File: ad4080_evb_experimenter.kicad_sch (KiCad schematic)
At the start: 61 parts, among them J1 Conn_Coaxial, J2 AudioJack2_Ground, J3 Conn_02x02_Odd_Even, J4 Conn_Coaxial, J5 Conn_Coaxial, SW1 SW_Coded_SH-7050, U1 LT1678, U2 74LS163, U3 74HC04, X1 CXO_DIP8

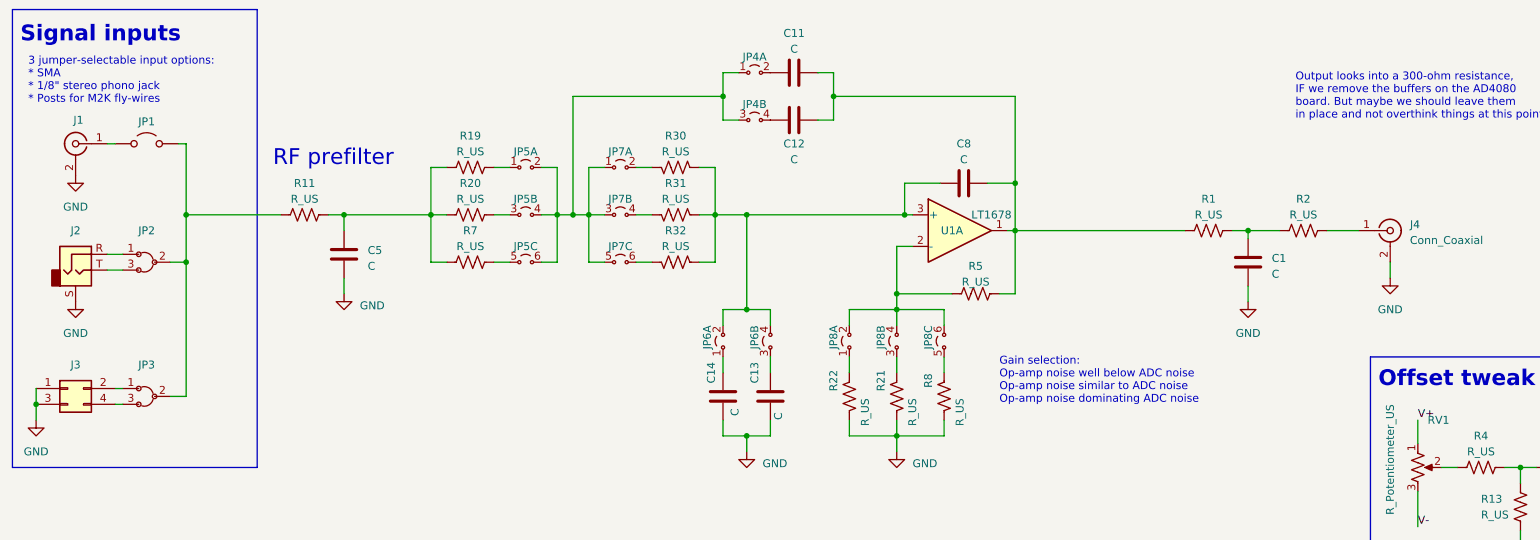
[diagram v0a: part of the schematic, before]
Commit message: Reduced unused space, fix DRC errors
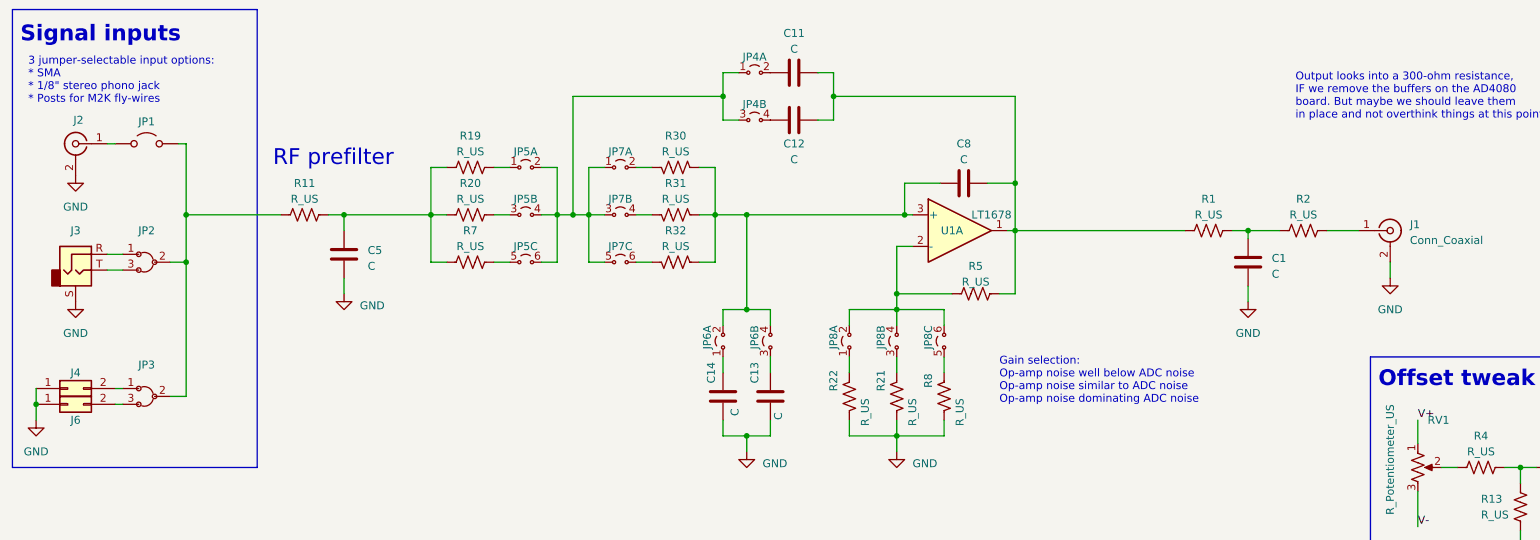
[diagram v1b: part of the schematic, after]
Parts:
- removed J3: Conn_02x02_Odd_Even, Connector_PinHeader_2.54mm:PinHeader_2x02_P2.54mm_Vertical, symbol Connector_Generic:Conn_02x02_Odd_Even
- added J4, J6: Conn_02x01, Connector_PinHeader_2.54mm:PinHeader_1x02_P2.54mm_Vertical, symbol Connector_Generic:Conn_02x01
- renumbered J4 to J1, J1 to J2, J2 to J3
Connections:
- net GND: now also J4.1 (Pin_1), J6.1 (Pin_1)
- net at JP3.1: now also J4.2 (Pin_2)
- net at JP3.3: now also J6.2 (Pin_2)
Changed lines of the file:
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@@
 	)
 	(junction
-		(at 17.78 77.47)
-		(diameter 0)
-		(color 0 0 0 0)
-	)
-	(junction
 		(at 49.53 120.65)
 		(diameter 0)
@@
 	)
 	(junction
+		(at 17.78 77.47)
+		(diameter 0)
+		(color 0 0 0 0)
+	)
+	(junction
 		(at 41.91 54.61)
 		(diameter 0)
@@
 	(wire
 		(pts
+			(xy 17.78 77.47) (xy 17.78 80.01)
+		)
+		(stroke
+			(width 0)
+			(type default)
+		)
+	)
+	(wire
+		(pts
 			(xy 62.23 120.65) (xy 57.15 120.65)
 		)
@@
 	(wire
 		(pts
-			(xy 17.78 77.47) (xy 17.78 80.01)
-		)
-		(stroke
-			(width 0)
-			(type default)
-		)
-	)
-	(wire
-		(pts
 			(xy 144.78 177.165) (xy 144.78 178.435)
 		)
@@
 		(dnp no)
 		(fields_autoplaced yes)
-		(property "Reference" "J4"
+		(property "Reference" "J1"
 			(at 238.76 48.5531 0)
 			(effects
@@
 			(project "ad4080_evb_experimenter"
 				(path "/b69282a1-dfbe-4b32-8ce1-82537d42439c"
-					(reference "J4")
+					(reference "J1")
 					(unit 1)
 				)
@@
 	)
 	(symbol
+		(lib_id "Connector_Generic:Conn_02x01")
+		(at 22.86 74.93 0)
+		(unit 1)
+		(exclude_from_sim no)
+		(in_bom yes)
+		(on_board yes)
+		(dnp no)
+		(property "Reference" "J4"
+			(at 24.13 72.39 0)
+			(effects
+				(font
+					(size 1.27 1.27)
+				)
+			)
+		)
+		(property "Value" "Conn_02x01"
+			(at 26.67 69.85 0)
+			(effects
+				(font
+					(size 1.27 1.27)
+				)
+				(hide yes)
+			)
+		)
+		(property "Footprint" "Connector_PinHeader_2.54mm:PinHeader_1x02_P2.54mm_Vertical"
+			(at 22.86 74.93 0)
+			(effects
+				(font
+					(size 1.27 1.27)
+				)
+				(hide yes)
+			)
+		)
+		(property "Datasheet" "~"
+			(at 22.86 74.93 0)
+			(effects
+				(font
+					(size 1.27 1.27)
+				)
+				(hide yes)
+			)
+		)
+		(property "Description" "Generic connector, double row, 02x01, this symbol is compatible with counter-clockwise, top-bottom and odd-even numbering schemes., script generated (kicad-library-utils/schlib/autogen/connector/)"
+			(at 22.86 74.93 0)
+			(effects
+				(font
+					(size 1.27 1.27)
+				)
+				(hide yes)
+			)
+		)
+		(pin "2"
+		)
+		(pin "1"
+		)
+		(instances
+			(project "ad4080_evb_experimenter"
+				(path "/b69282a1-dfbe-4b32-8ce1-82537d42439c"
+					(reference "J4")
+					(unit 1)
+				)
+			)
+		)
+	)
+	(symbol
 		(lib_id "74xx:74HC04")
 		(at 128.27 174.625 0)
@@
 		(on_board yes)
 		(dnp no)
-		(property "Reference" "J1"
+		(property "Reference" "J2"
 			(at 25.4 31.75 0)
 			(effects
@@
 			(project "ad4080_evb_experimenter"
 				(path "/b69282a1-dfbe-4b32-8ce1-82537d42439c"
-					(reference "J1")
+					(reference "J2")
 					(unit 1)
 				)
@@
 	)
 	(symbol
-		(lib_id "Connector_Generic:Conn_02x02_Odd_Even")
-		(at 22.86 74.93 0)
-		(unit 1)
-		(exclude_from_sim no)
-		(in_bom yes)
-		(on_board yes)
-		(dnp no)
-		(property "Reference" "J3"
-			(at 24.13 71.12 0)
-			(effects
-				(font
-					(size 1.27 1.27)
-				)
-			)
-		)
-		(property "Value" "Conn_02x02_Odd_Even"
-			(at 24.13 71.12 0)
-			(effects
-				(font
-					(size 1.27 1.27)
-				)
-				(hide yes)
-			)
-		)
-		(property "Footprint" "Connector_PinHeader_2.54mm:PinHeader_2x02_P2.54mm_Vertical"
-			(at 22.86 74.93 0)
-			(effects
-				(font
-					(size 1.27 1.27)
-				)
-				(hide yes)
-			)
-		)
-		(property "Datasheet" "~"
-			(at 22.86 74.93 0)
-			(effects
-				(font
-					(size 1.27 1.27)
-				)
-				(hide yes)
-			)
-		)
-		(property "Description" "Generic connector, double row, 02x02, odd/even pin numbering scheme (row 1 odd numbers, row 2 even numbers), script generated (kicad-library-utils/schlib/autogen/connector/)"
-			(at 22.86 74.93 0)
-			(effects
-				(font
-					(size 1.27 1.27)
-				)
-				(hide yes)
-			)
-		)
-		(pin "4"
-		)
-		(pin "3"
-		)
-		(pin "1"
-		)
-		(pin "2"
-		)
-		(instances
-			(project "ad4080_evb_experimenter"
-				(path "/b69282a1-dfbe-4b32-8ce1-82537d42439c"
-					(reference "J3")
-					(unit 1)
-				)
-			)
-		)
-	)
-	(symbol
 		(lib_id "Amplifier_Operational:LM358")
 		(at 166.37 49.53 0)
@@
 	)
 	(symbol
+		(lib_id "Connector_Generic:Conn_02x01")
+		(at 22.86 77.47 0)
+		(unit 1)
+		(exclude_from_sim no)
+		(in_bom yes)
+		(on_board yes)
+		(dnp no)
+		(property "Reference" "J6"
+			(at 24.13 80.01 0)
+			(effects
+				(font
+					(size 1.27 1.27)
+				)
+			)
+		)
+		(property "Value" "Conn_02x01"
+			(at 27.94 82.55 0)
+			(effects
+				(font
+					(size 1.27 1.27)
+				)
+				(hide yes)
+			)
+		)
+		(property "Footprint" "Connector_PinHeader_2.54mm:PinHeader_1x02_P2.54mm_Vertical"
+			(at 22.86 77.47 0)
+			(effects
+				(font
+					(size 1.27 1.27)
+				)
+				(hide yes)
+			)
+		)
+		(property "Datasheet" "~"
+			(at 22.86 77.47 0)
+			(effects
+				(font
+					(size 1.27 1.27)
+				)
+				(hide yes)
+			)
+		)
+		(property "Description" "Generic connector, double row, 02x01, this symbol is compatible with counter-clockwise, top-bottom and odd-even numbering schemes., script generated (kicad-library-utils/schlib/autogen/connector/)"
+			(at 22.86 77.47 0)
+			(effects
+				(font
+					(size 1.27 1.27)
+				)
+				(hide yes)
+			)
+		)
+		(pin "2"
+		)
+		(pin "1"
+		)
+		(instances
+			(project "ad4080_evb_experimenter"
+				(path "/b69282a1-dfbe-4b32-8ce1-82537d42439c"
+					(reference "J6")
+					(unit 1)
+				)
+			)
+		)
+	)
+	(symbol
 		(lib_id "Device:R_US")
 		(at 256.54 93.98 180)
@@
 		(on_board yes)
 		(dnp no)
-		(property "Reference" "J2"
+		(property "Reference" "J3"
 			(at 24.13 49.53 0)
 			(effects
@@
 			(project "ad4080_evb_experimenter"
 				(path "/b69282a1-dfbe-4b32-8ce1-82537d42439c"
-					(reference "J2")
+					(reference "J3")
 					(unit 1)
 				)

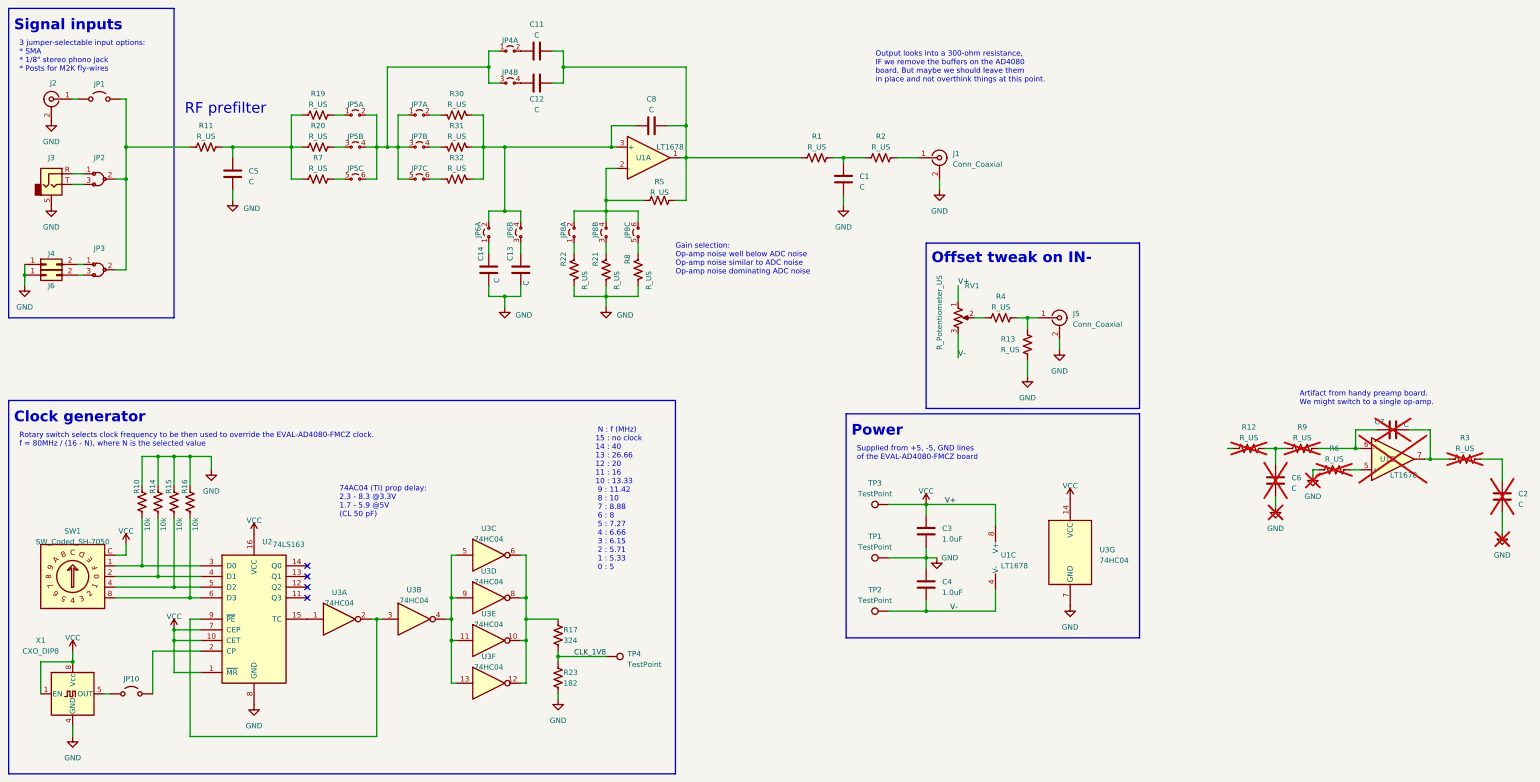
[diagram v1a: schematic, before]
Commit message: Single opamp, decouple digital power, selectable attenuation, routing and silkscreen tweaks
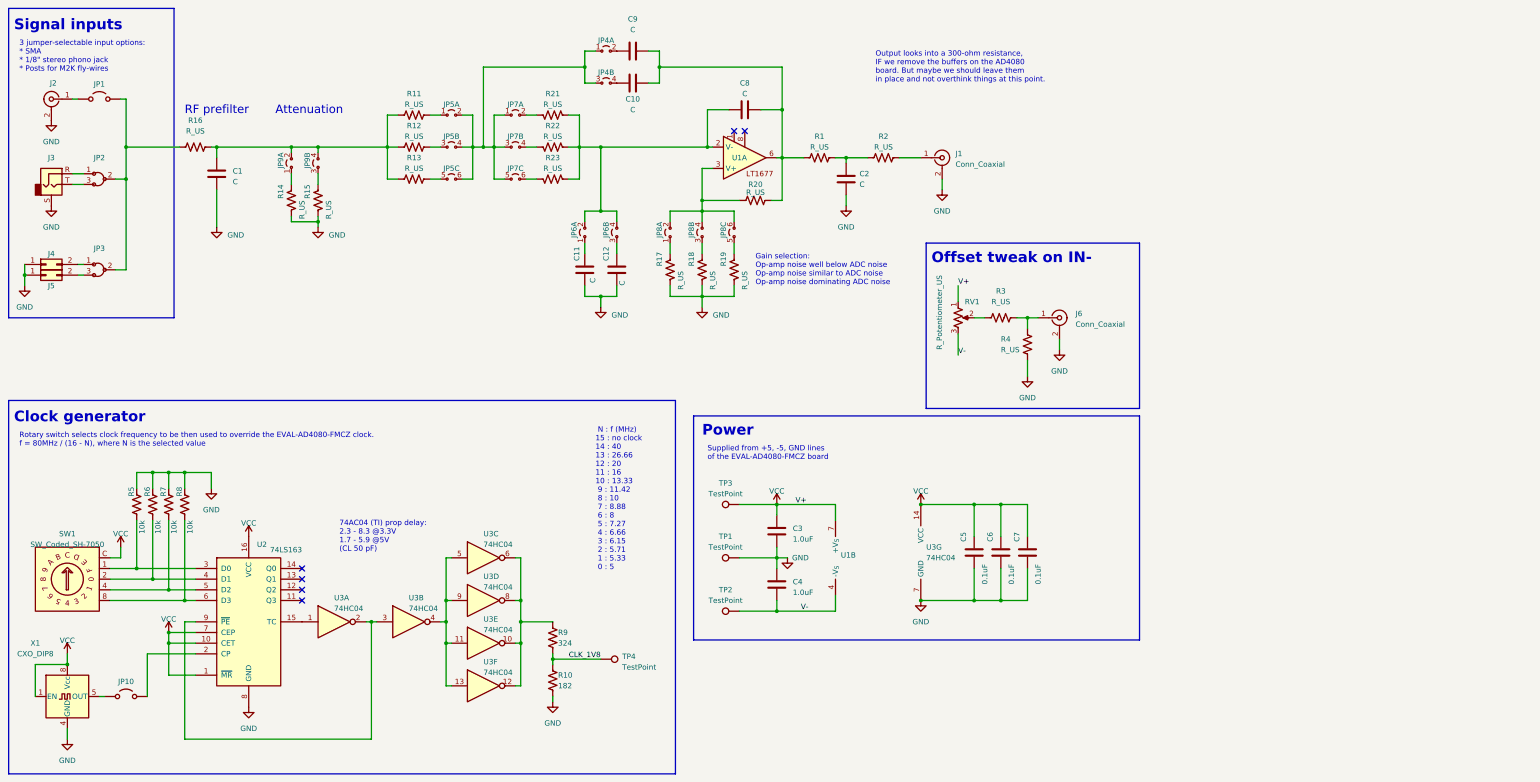
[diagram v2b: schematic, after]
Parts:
- removed C2: C, Capacitor_THT:C_Rect_L7.2mm_W2.5mm_P5.00mm_FKS2_FKP2_MKS2_MKP2, symbol Device:C
- removed R12, R3, R6, R9: R_US, Resistor_THT:R_Axial_DIN0207_L6.3mm_D2.5mm_P10.16mm_Horizontal, symbol Device:R_US
- removed U1: LT1678, Package_DIP:DIP-8_W7.62mm_LongPads, symbol Amplifier_Operational:LM358
- added C5: 0.1uF, Capacitor_THT:C_Rect_L7.2mm_W2.5mm_P5.00mm_FKS2_FKP2_MKS2_MKP2, symbol Device:C
- added JP9: ~, Connector_PinHeader_2.54mm:PinHeader_2x02_P2.54mm_Vertical, symbol FTC2024:JumperBlock_2x2
- added R14, R15: R_US, Resistor_THT:R_Axial_DIN0207_L6.3mm_D2.5mm_P10.16mm_Horizontal, symbol Device:R_US
- added U1: ~, Package_DIP:DIP-8_W7.62mm, symbol FTC2024:LT1677
- C6, C7: value C -> 0.1uF; now fitted; now in the parts list
- JP2, JP3: symbol FTC2024:Jumper3 -> FTC2024:Jumper_3
- renumbered C5 to C1, C12 to C10, C14 to C11, C13 to C12, C1 to C2, C11 to C9, J6 to J5, J5 to J6, R23 to R10, R19 to R11, R20 to R12, R7 to R13, R11 to R16, R22 to R17, R21 to R18, R8 to R19, R5 to R20, R30 to R21, R31 to R22, R32 to R23, R4 to R3, R13 to R4, R10 to R5, R14 to R6, R15 to R7, R16 to R8, R17 to R9
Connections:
- net GND: now also C7.2, C5.2, R14.1, R15.1
- net V-: now also U1.4 (-V_{S})
- net VCC: now also C6.1, C7.1, C5.1, U1.7 (+V_{S})
- net at JP8.2, JP8.4, JP8.6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: now also U1.3 (V+)
- net at C8.1, JP6.2, JP6.4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: now also U1.2 (V-)
- net at C1.1, R11.1, R12.1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: now also JP9.2, JP9.4
- net at C10.2, C8.2, C9.2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: now also U1.6
- new net: JP9.1, R14.2
- new net: JP9.3, R15.2
- no-connect marks 4 -> 6
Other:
- note added: "Attenuation"
- note removed: "Artifact from handy preamp board. We might switch to a single op-amp."
- moved on the sheet: C1, C10, C11, C12, C2, C3, C4, C8, C9, J1, JP10, JP4A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

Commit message: Fix flipped opamp inputs
Signed-off-by: Ioan Dragomir <ioan.dragomir@analog.com>
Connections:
- net at JP8.2, JP8.4, JP8.6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: now also U1.2 (V-); no longer U1.3 (V+)
- net at C8.1, JP6.2, JP6.4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: now also U1.3 (V+); no longer U1.2 (V-)
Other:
- moved on the sheet: U1A
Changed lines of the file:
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@@
 	)
 	(no_connect
-		(at 186.69 43.18)
+		(at 186.69 55.88)
 	)
 	(no_connect
-		(at 189.23 43.18)
+		(at 189.23 55.88)
 	)
 	(no_connect
@@
 		(lib_id "FTC2024:LT1677")
 		(at 184.15 49.53 0)
+		(mirror x)
 		(unit 1)
 		(exclude_from_sim no)
@@
 		)
 		(property "Value" "~"
-			(at 190.1685 58.42 0)
+			(at 190.1685 40.64 0)
 			(effects
 				(font

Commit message: Change test points to smaller Keystone Miniature
Signed-off-by: Ioan Dragomir <ioan.dragomir@analog.com>
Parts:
- TP1, TP2, TP3: footprint TestPoint:TestPoint_Plated_Hole_D3.0mm -> TestPoint:TestPoint_Keystone_5005-5009_Compact
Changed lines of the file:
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@@
 			)
 		)
-		(property "Footprint" "TestPoint:TestPoint_Plated_Hole_D3.0mm"
+		(property "Footprint" "TestPoint:TestPoint_Keystone_5005-5009_Compact"
 			(at 187.96 152.4 0)
 			(effects
@@
 			)
 		)
-		(property "Footprint" "TestPoint:TestPoint_Plated_Hole_D3.0mm"
+		(property "Footprint" "TestPoint:TestPoint_Keystone_5005-5009_Compact"
 			(at 187.96 139.7 0)
 			(effects
@@
 			)
 		)
-		(property "Footprint" "TestPoint:TestPoint_Plated_Hole_D3.0mm"
+		(property "Footprint" "TestPoint:TestPoint_Keystone_5005-5009_Compact"
 			(at 187.96 127 0)
 			(effects

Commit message: Add mounting holes, 3mm
Signed-off-by: Ioan Dragomir <ioan.dragomir@analog.com>
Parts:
- added H1, H2: MountingHole_Pad, MountingHole:MountingHole_3mm_Pad, symbol Mechanical:MountingHole_Pad
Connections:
- net GND: now also H1.1, H2.1
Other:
- note added: "Mounting holes"
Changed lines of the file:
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@@
 	)
 	(junction
+		(at 19.05 99.06)
+		(diameter 0)
+		(color 0 0 0 0)
+	)
+	(junction
 		(at 168.91 27.94)
 		(diameter 0)
@@
 	(wire
 		(pts
+			(xy 19.05 99.06) (xy 24.13 99.06)
+		)
+		(stroke
+			(width 0)
+			(type default)
+		)
+	)
+	(wire
+		(pts
 			(xy 135.89 144.78) (xy 135.89 154.94)
 		)
@@
 		)
 	)
+	(text "Mounting holes"
+		(exclude_from_sim no)
+		(at 22.86 91.44 0)
+		(effects
+			(font
+				(size 1.27 1.27)
+			)
+		)
+	)
 	(text "Supplied from +5, -5, GND lines\nof the EVAL-AD4080-FMCZ board"
 		(exclude_from_sim no)
@@
 	)
 	(symbol
+		(lib_id "Mechanical:MountingHole_Pad")
+		(at 19.05 96.52 0)
+		(unit 1)
+		(exclude_from_sim yes)
+		(in_bom no)
+		(on_board yes)
+		(dnp no)
+		(property "Reference" "H1"
+			(at 21.59 93.9799 0)
+			(effects
+				(font
+					(size 1.27 1.27)
+				)
+				(justify left)
+				(hide yes)
+			)
+		)
+		(property "Value" "MountingHole_Pad"
+			(at 10.16 91.44 0)
+			(effects
+				(font
+					(size 1.27 1.27)
+				)
+				(justify left)
+				(hide yes)
+			)
+		)
+		(property "Footprint" "MountingHole:MountingHole_3mm_Pad"
+			(at 19.05 96.52 0)
+			(effects
+				(font
+					(size 1.27 1.27)
+				)
+				(hide yes)
+			)
+		)
+		(property "Datasheet" "~"
+			(at 19.05 96.52 0)
+			(effects
+				(font
+					(size 1.27 1.27)
+				)
+				(hide yes)
+			)
+		)
+		(property "Description" "Mounting Hole with connection"
+			(at 19.05 96.52 0)
+			(effects
+				(font
+					(size 1.27 1.27)
+				)
+				(hide yes)
+			)
+		)
+		(pin "1"
+		)
+		(instances
+			(project "ad4080_evb_experimenter"
+				(path "/b69282a1-dfbe-4b32-8ce1-82537d42439c"
+					(reference "H1")
+					(unit 1)
+				)
+			)
+		)
+	)
+	(symbol
+		(lib_id "power:GND")
+		(at 19.05 99.06 0)
+		(unit 1)
+		(exclude_from_sim no)
+		(in_bom yes)
+		(on_board yes)
+		(dnp no)
+		(fields_autoplaced yes)
+		(property "Reference" "#PWR09"
+			(at 19.05 105.41 0)
+			(effects
+				(font
+					(size 1.27 1.27)
+				)
+				(hide yes)
+			)
+		)
+		(property "Value" "GND"
+			(at 21.59 100.965 0)
+			(effects
+				(font
+					(size 1.27 1.27)
+				)
+				(justify left)
+			)
+		)
+		(property "Footprint" ""
+			(at 19.05 99.06 0)
+			(effects
+				(font
+					(size 1.27 1.27)
+				)
+				(hide yes)
+			)
+		)
+		(property "Datasheet" ""
+			(at 19.05 99.06 0)
+			(effects
+				(font
+					(size 1.27 1.27)
+				)
+				(hide yes)
+			)
+		)
+		(property "Description" ""
+			(at 19.05 99.06 0)
+			(effects
+				(font
+					(size 1.27 1.27)
+				)
+				(hide yes)
+			)
+		)
+		(pin "1"
+		)
+		(instances
+			(project "ad4080_evb_experimenter"
+				(path "/b69282a1-dfbe-4b32-8ce1-82537d42439c"
+					(reference "#PWR09")
+					(unit 1)
+				)
+			)
+		)
+	)
+	(symbol
 		(lib_id "Device:R_US")
 		(at 110.49 54.61 90)
@@
 					(unit 1)
 				)
+			)
+		)
+	)
+	(symbol
+		(lib_id "Mechanical:MountingHole_Pad")
+		(at 24.13 96.52 0)
+		(unit 1)
+		(exclude_from_sim yes)
+		(in_bom no)
+		(on_board yes)
+		(dnp no)
+		(fields_autoplaced yes)
+		(property "Reference" "H2"
+			(at 26.67 93.9799 0)
+			(effects
+				(font
+					(size 1.27 1.27)
+				)
+				(justify left)
+				(hide yes)
+			)
+		)
+		(property "Value" "MountingHole_Pad"
+			(at 26.67 96.5199 0)
+			(effects
+				(font
+					(size 1.27 1.27)
+				)
+				(justify left)
+				(hide yes)
+			)
+		)
+		(property "Footprint" "MountingHole:MountingHole_3mm_Pad"
+			(at 24.13 96.52 0)
+			(effects
+				(font
+					(size 1.27 1.27)
+				)
+				(hide yes)
+			)
+		)
+		(property "Datasheet" "~"
+			(at 24.13 96.52 0)
+			(effects
+				(font
+					(size 1.27 1.27)
+				)
+				(hide yes)
+			)
+		)
+		(property "Description" "Mounting Hole with connection"
+			(at 24.13 96.52 0)
+			(effects
+				(font
+					(size 1.27 1.27)
+				)
+				(hide yes)
+			)
+		)
+		(pin "1"
+		)
+		(instances
+			(project "ad4080_evb_experimenter"
+				(path "/b69282a1-dfbe-4b32-8ce1-82537d42439c"
+					(reference "H2")
+					(unit 1)
+				)
